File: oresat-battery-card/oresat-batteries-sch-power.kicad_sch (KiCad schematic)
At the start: 86 parts, among them Q1 DMP2240UDM-7, Q2 DMN2053UQ-13, Q3 DMP3050LVTQ-7, Q4 DMP3050LVTQ-7, Q44 DMN2053UQ-13, Q5 DMN2053UQ-13, U1 MAX7310, U2 MIC842LYC5, U3 MIC842LYC5, U4 MAX4211, U5 TPS62111RSA, U6 TS5A21366DCUR

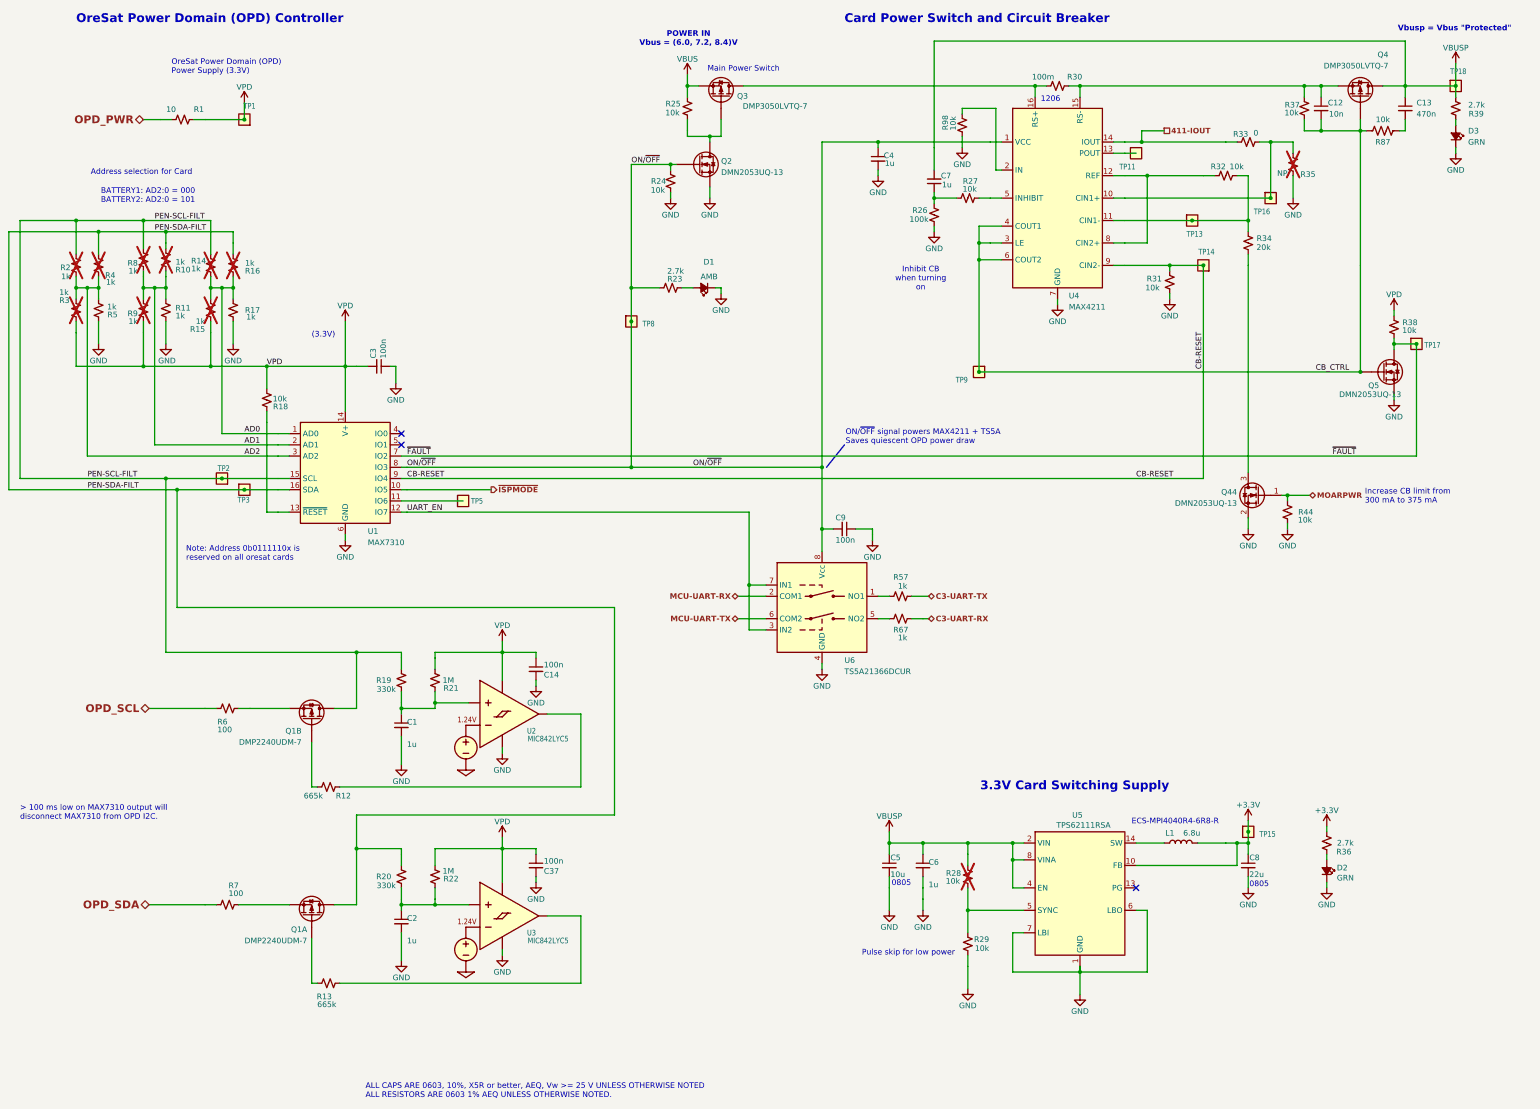
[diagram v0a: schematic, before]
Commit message: Jumped back on the TPS bandwagon - LCSC to the rescue! - and lots of cleanup.
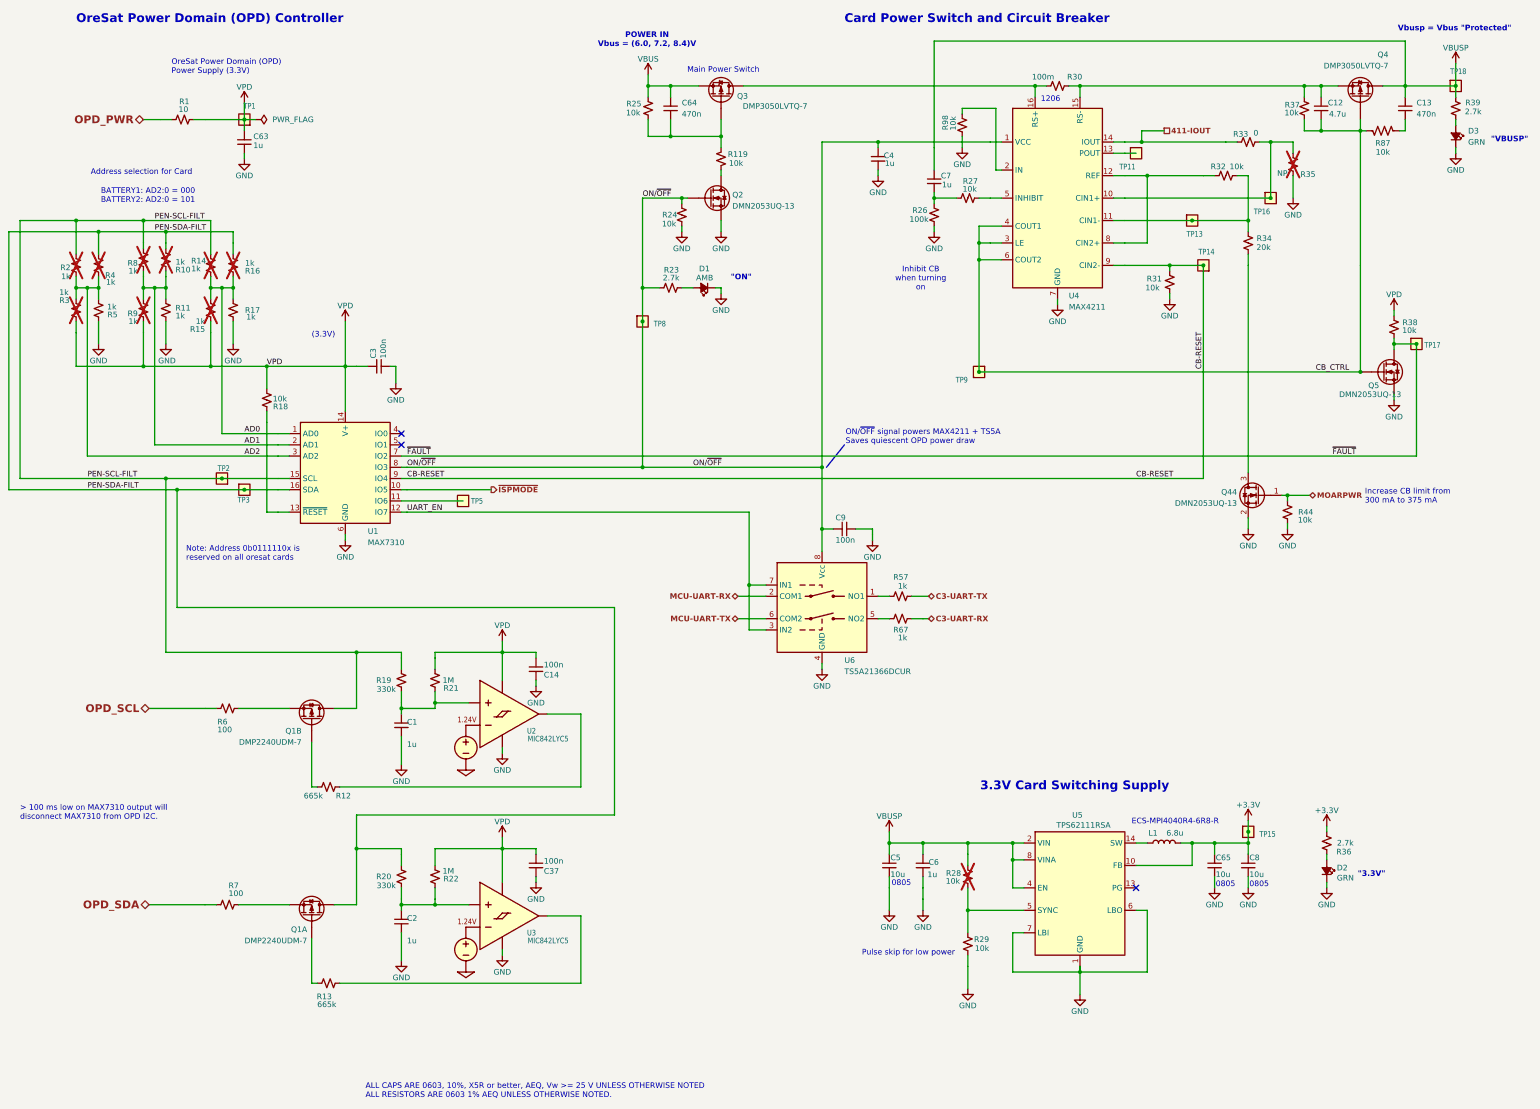
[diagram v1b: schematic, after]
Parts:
- added C63: 1u, oresat-passives:0603-C-NOSILK, symbol Device:C_Small
- added C64: 470n, oresat-passives:0603-C-NOSILK, symbol Device:C_Small
- added C65: 10u, oresat-passives:0805-C-NOSILK, symbol Device:C_Small
- added R119: 10k, oresat-passives:0603-C-NOSILK, symbol Device:R_Small_US
- C12: value 10n -> 4.7u; footprint oresat-passives:0603-C-NOSILK -> oresat-passives:0805-C-NOSILK; DPN 399-12983-1-ND -> (none); MFR KEMET -> (none); MPN C0603C103J5RACAUTO -> (none)
- C8: value 22u -> 10u; DPN 490-GRT21BC81C226ME13LCT-ND -> 490-GRT21BC71E106KE13KCT-ND; MPN GRT21BC81C226ME13L -> GRT21BC71E106KE13K
- R11, R17, R5, R57, R67: DPN RMCF0603FT2K70CT-ND -> RMCF0603FT1K00CT-ND
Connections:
- net +3.3V: now also C65.1
- net GND: now also C63.2, C65.2
- net VBUS: now also C64.1
- net VPD: now also C63.1
- net at Q3.3 (G), R25.1: now also C64.2, R119.2; no longer Q2.3 (D)
- new net: Q2.3 (D), R119.1
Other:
- note added: ""3.3V""
- note added: ""ON""
- note added: ""VBUSP""
- moved on the sheet: L1, Q2, R24, R25, TP8

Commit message: Battery Card 4.0, no ERC or DRC errors or warnings
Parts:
- C12: DPN (none) -> 490-GRT21BC71E475KE13LCT-ND; MFR (none) -> Murata Electronics; MPN (none) -> GRT21BC71E475KE13L
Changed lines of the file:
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@@
 	(title_block
 		(title "OreSat Battery Card")
-		(date "2026-09-27")
+		(date "2026-10-06")
 		(rev "4.0")
 		(company "Portland State Aerospace Society")
@@
 			)
 		)
-		(property "Datasheet" ""
+		(property "Datasheet" "https://search.murata.co.jp/Ceramy/image/img/A01X/G101/ENG/GRT21BC71E475KE13-01.pdf"
 			(at 328.93 41.91 0)
 			(hide yes)
@@
 			)
 		)
-		(property "Description" ""
+		(property "Description" "4.7 µF ±10% 25V Ceramic Capacitor X7S 0805 (2012 Metric)"
 			(at 328.93 41.91 0)
 			(hide yes)
@@
 			)
 		)
-		(property "DPN" ""
+		(property "DPN" "490-GRT21BC71E475KE13LCT-ND"
 			(at 328.93 41.91 0)
 			(hide yes)
@@
 			)
 		)
-		(property "MFR" ""
+		(property "MFR" "Murata Electronics"
 			(at 328.93 41.91 0)
 			(hide yes)
@@
 			)
 		)
-		(property "MPN" ""
+		(property "MPN" "GRT21BC71E475KE13L"
 			(at 328.93 41.91 0)
 			(hide yes)

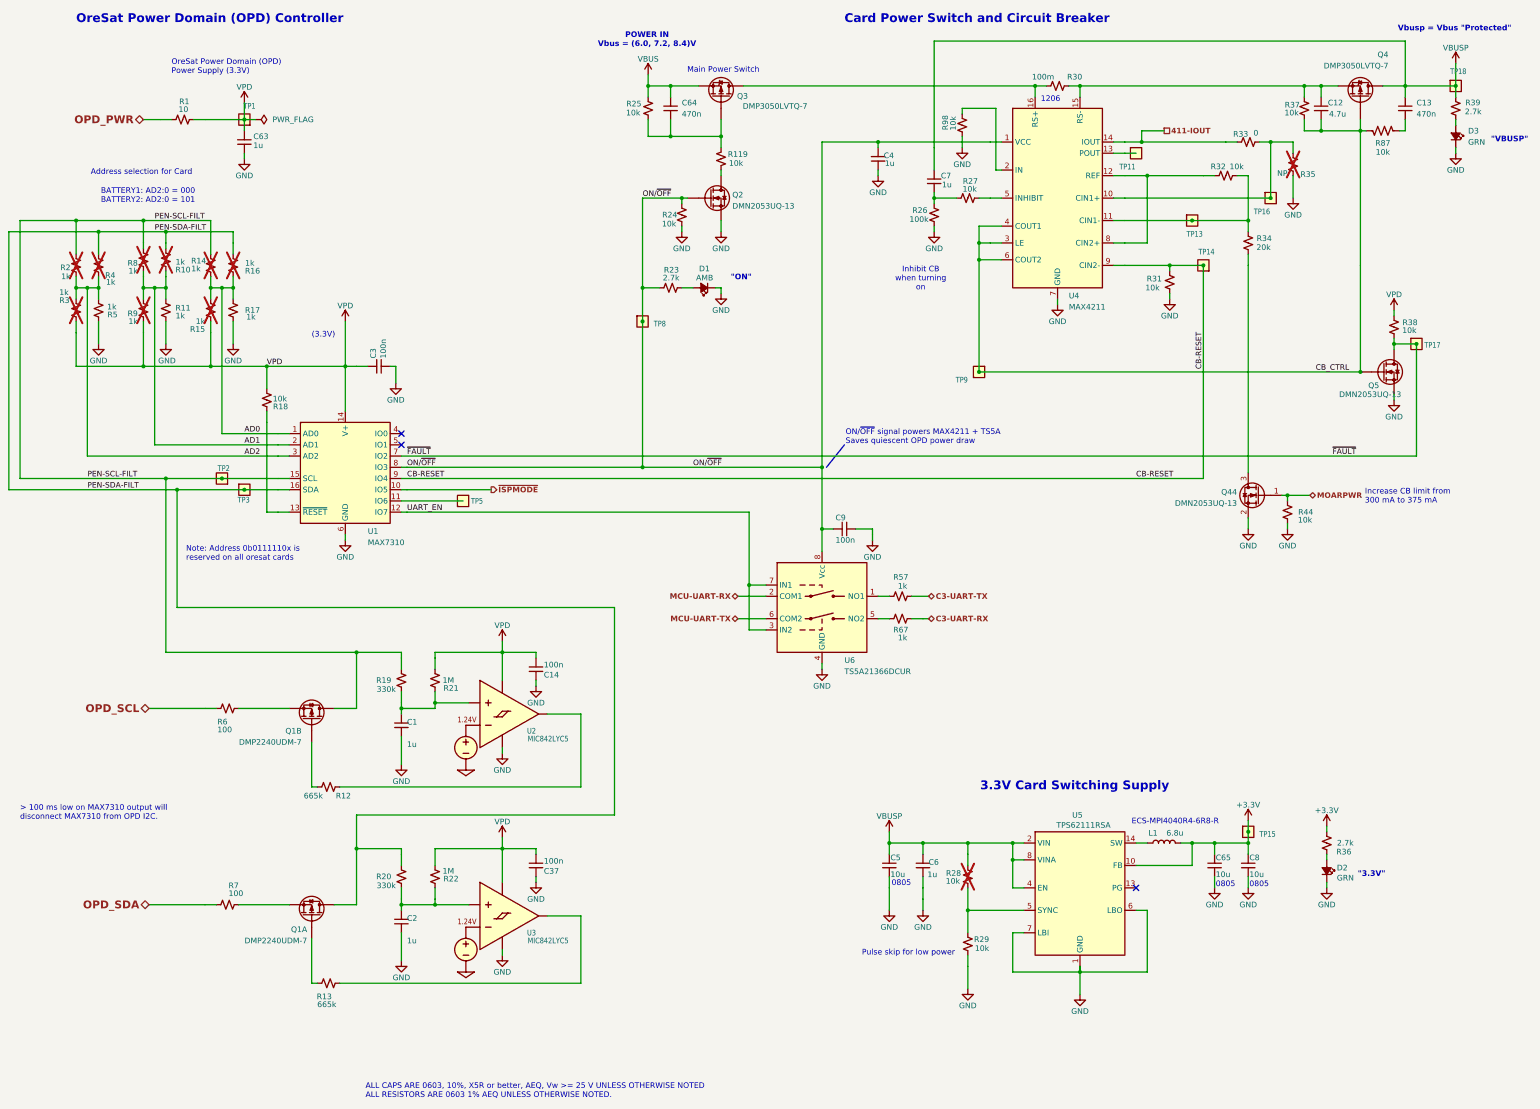
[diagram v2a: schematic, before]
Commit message: Updated Makefile and Readme; fixed TCAN IC, cleanup, fix battery connections that were killed somehow
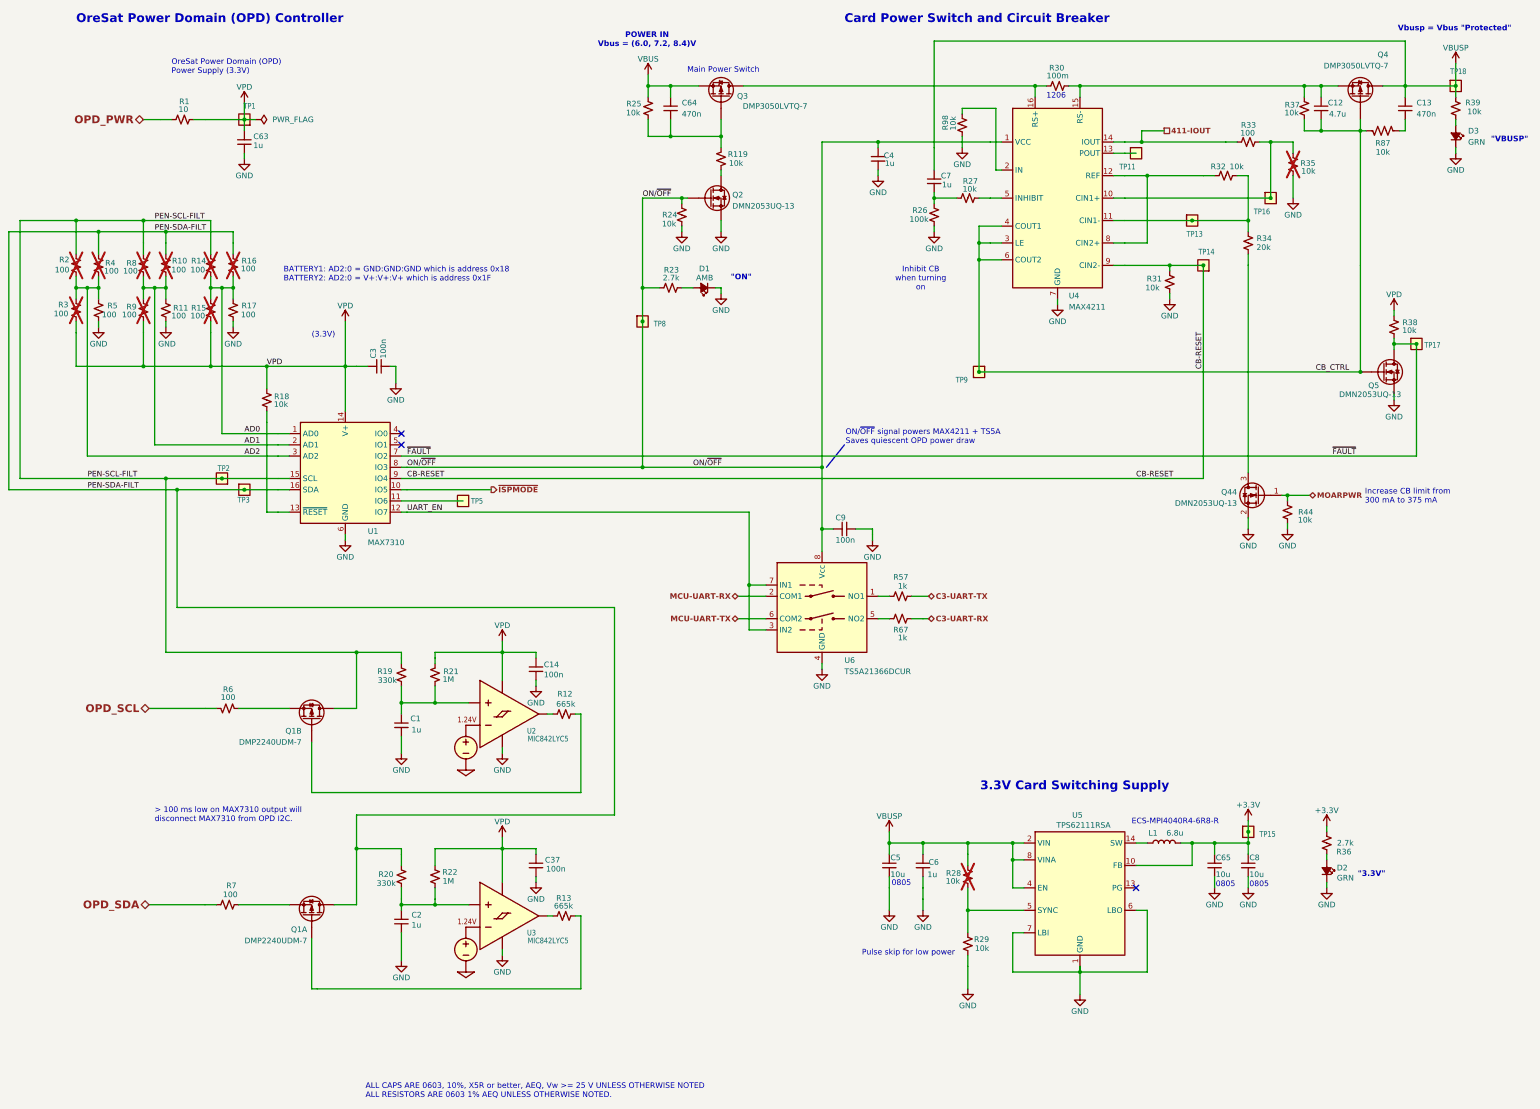
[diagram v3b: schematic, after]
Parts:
- R10, R14, R15, R16, R2, R3, R4, R8, R9: value 1k -> 100; DPN RMCF0603FT2K70CT-ND -> RMCF0603FT100RCT-ND; MPN RMCF0603FT1K00 -> RMCF0603FT100R
- R11, R17, R5: value 1k -> 100; DPN RMCF0603FT1K00CT-ND -> RMCF0603FT100RCT-ND; MPN RMCF0603FT1K00 -> RMCF0603FT100R
- R33: value 0 -> 100; DPN RMCF0603ZT0R00CT-ND -> RMCF0603FT100RCT-ND; MPN RMCF0603ZT0R00 -> RMCF0603FT100R
- R35: value NP -> 10k
- R39: value 2.7k -> 10k; DPN RMCF0603FT2K70CT-ND -> RMCF0603FT10K0CT-ND; MPN RMCF0603FT2K70 -> RMCF0603FT10K0
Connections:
- net GND: now also C14.1; no longer C14.2
- net VPD: now also C14.2, R21.1; no longer C14.1, R21.2
- net at C1.1, R19.1, U2.1 (INP): now also R21.2; no longer R21.1
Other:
- note added: "BATTERY1: AD2:0 = GND:GND:GND which is address 0x18 BATTERY2: AD2:0 = V+:V+:V+ which is address 0x1F"
- note removed: "Address selection for Card"
- note removed: "BATTERY1: AD2:0 = 000 BATTERY2: AD2:0 = 101"
- note removed: "Note: Address 0b0111110x is reserved on all oresat cards"
- moved on the sheet: R10, R12, R13, R19, R21, R8

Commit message: Changes to eFuse after trying evaluation board, and recalculating values, and trying to reduce number of passive components to minimum number
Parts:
- R34: value 20k -> 10k; DPN RMCF0603FT20K0CT-ND -> RMCF0603FT10K0CT-ND; MPN RMCF0603FT20K0 -> RMCF0603FT10K0
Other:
- note added: "Increase CB limit from 300 mA to 600 mA in order to run the heaters."
- note removed: "Increase CB limit from 300 mA to 375 mA"
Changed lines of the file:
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@@
 		)
 	)
-	(text "Increase CB limit from\n300 mA to 375 mA"
+	(text "Increase CB limit from\n300 mA to 600 mA\nin order to run the heaters."
 		(exclude_from_sim no)
 		(at 338.836 131.572 0)
@@
 			)
 		)
-		(property "Value" "20k"
+		(property "Value" "10k"
 			(at 317.5 72.644 0)
 			(show_name no)
@@
 			)
 		)
-		(property "Description" "20 kOhms ±1% 0.1W, 1/10W Chip Resistor 0603 (1608 Metric) Automotive AEC-Q200 Thick Film"
+		(property "Description" "10 kOhms ±1% 0.1W, 1/10W Chip Resistor 0603 (1608 Metric) Automotive AEC-Q200 Thick Film"
 			(at 312.42 72.39 0)
 			(hide yes)
@@
 			)
 		)
-		(property "DPN" "RMCF0603FT20K0CT-ND"
+		(property "DPN" "RMCF0603FT10K0CT-ND"
 			(at 312.42 72.39 0)
 			(hide yes)
@@
 			)
 		)
-		(property "MPN" "RMCF0603FT20K0"
+		(property "MPN" "RMCF0603FT10K0"
 			(at 312.42 72.39 0)
 			(hide yes)

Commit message: Changes after inventory check and BOM check
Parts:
- C13, C64: DPN 399-6820-1-ND -> 399-C0603C474K3RACAUTOCT-ND; MPN C0603C473K5RACAUTO -> C0603C474K3RACAUTO
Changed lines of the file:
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@@
 			)
 		)
-		(property "Datasheet" "https://search.kemet.com/download/specsheet/C0603C473K5RACAUTO"
+		(property "Datasheet" "https://www.yageogroup.com/content/datasheet/asset/file/KEM_C1023_X7R_AUTO_SMD"
 			(at 181.61 41.91 0)
 			(hide yes)
@@
 			)
 		)
-		(property "Description" "0.047 µF ±10% 50V Ceramic Capacitor X7R 0603 (1608 Metric)"
+		(property "Description" "0.47 µF ±10% 25V Ceramic Capacitor X7R 0603 (1608 Metric)"
 			(at 181.61 41.91 0)
 			(hide yes)
@@
 			)
 		)
-		(property "DPN" "399-6820-1-ND"
+		(property "DPN" "399-C0603C474K3RACAUTOCT-ND"
 			(at 181.61 41.91 0)
 			(hide yes)
@@
 			)
 		)
-		(property "MPN" "C0603C473K5RACAUTO"
+		(property "MPN" "C0603C474K3RACAUTO"
 			(at 181.61 41.91 0)
 			(hide yes)
@@
 			)
 		)
-		(property "Datasheet" "https://search.kemet.com/download/specsheet/C0603C473K5RACAUTO"
+		(property "Datasheet" "https://www.yageogroup.com/content/datasheet/asset/file/KEM_C1023_X7R_AUTO_SMD"
 			(at 347.98 41.91 0)
 			(hide yes)
@@
 			)
 		)
-		(property "Description" "0.047 µF ±10% 50V Ceramic Capacitor X7R 0603 (1608 Metric)"
+		(property "Description" "0.47 µF ±10% 25V Ceramic Capacitor X7R 0603 (1608 Metric)"
 			(at 347.98 41.91 0)
 			(hide yes)
@@
 			)
 		)
-		(property "DPN" "399-6820-1-ND"
+		(property "DPN" "399-C0603C474K3RACAUTOCT-ND"
 			(at 347.98 41.91 0)
 			(hide yes)
@@
 			)
 		)
-		(property "MPN" "C0603C473K5RACAUTO"
+		(property "MPN" "C0603C474K3RACAUTO"
 			(at 347.98 41.91 0)
 			(hide yes)
